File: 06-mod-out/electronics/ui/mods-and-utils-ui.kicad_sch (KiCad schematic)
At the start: 23 parts, among them J1 Conn_02x03_Odd_Even, J3 Conn_02x03_Odd_Even, J4 Conn_01x02, J5 Conn_01x06, J6 Conn_02x03_Odd_Even, J8 Conn_02x03_Odd_Even

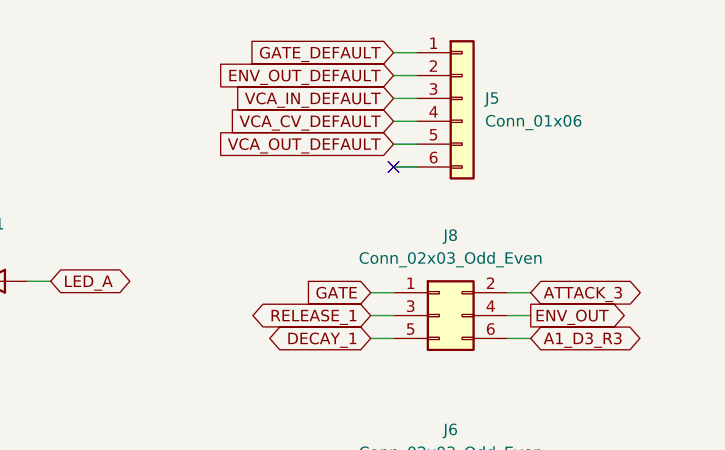
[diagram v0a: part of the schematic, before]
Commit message: Added double defaults pin row to ADSR
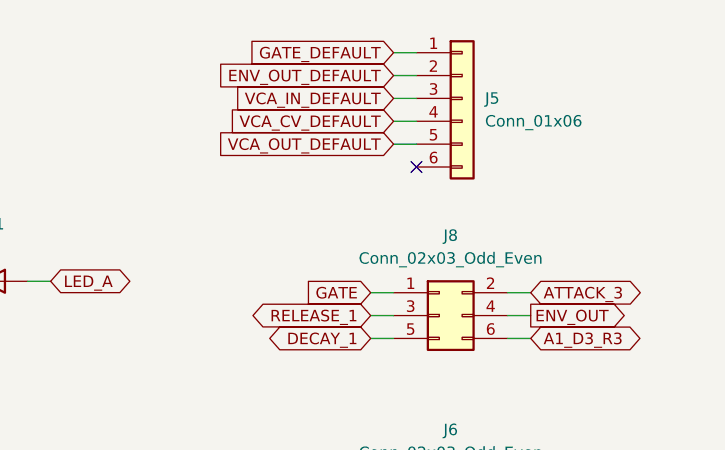
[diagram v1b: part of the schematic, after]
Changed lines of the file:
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@@
 	)
 	(no_connect
-		(at 245.11 41.91)
+		(at 247.65 41.91)
 	)
 	(no_connect
@@
 		)
 		(stroke
-			(width 0)
-			(type default)
-		)
-	)
-	(wire
-		(pts
-			(xy 245.11 41.91) (xy 247.65 41.91)
-		)
-		(stroke
